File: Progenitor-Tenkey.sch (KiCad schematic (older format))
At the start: 208 parts, among them SW1 SW_Push, U1 ATmega32U4-AU, Y1 16MHz

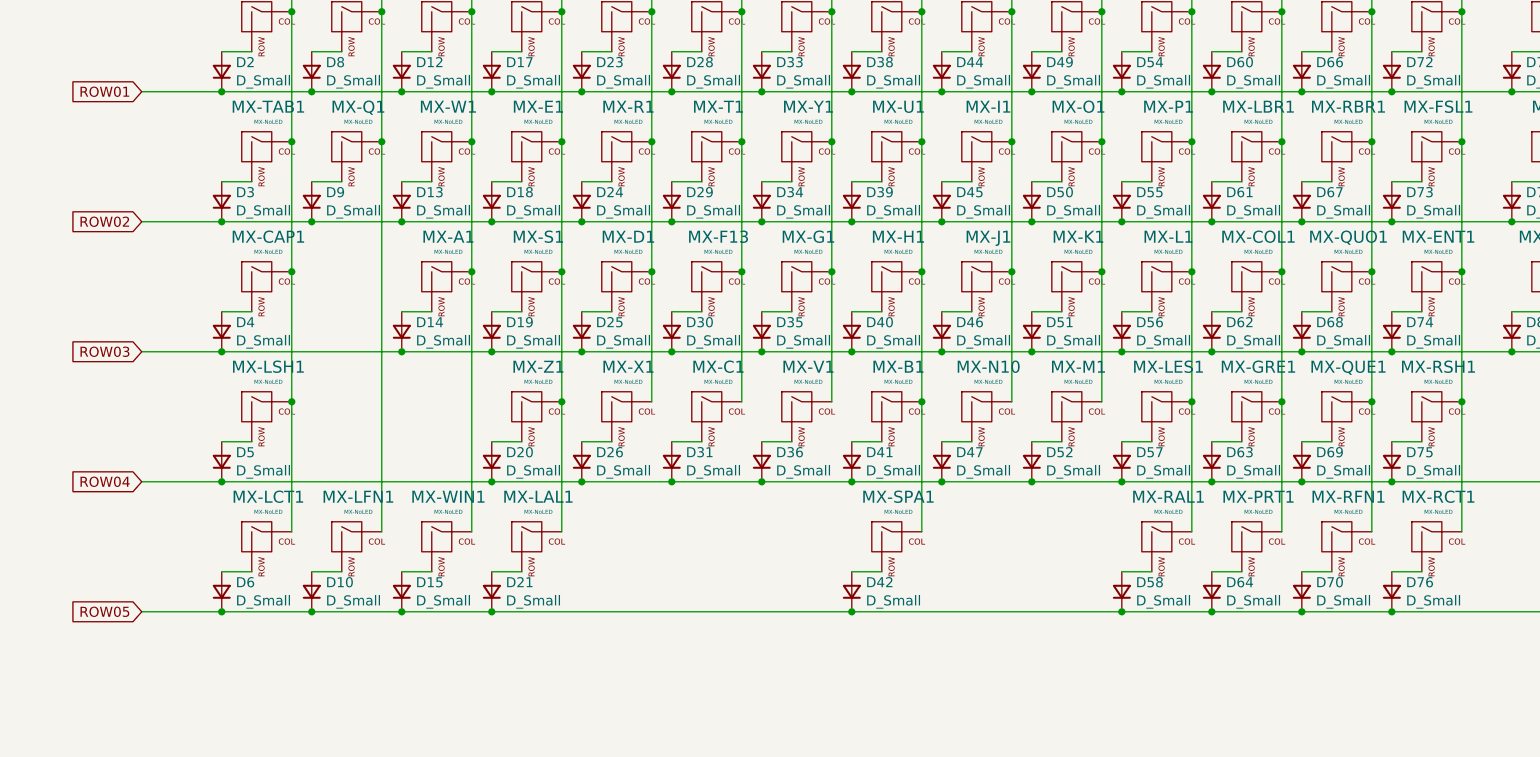
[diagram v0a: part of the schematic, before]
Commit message: Assigned Footprints
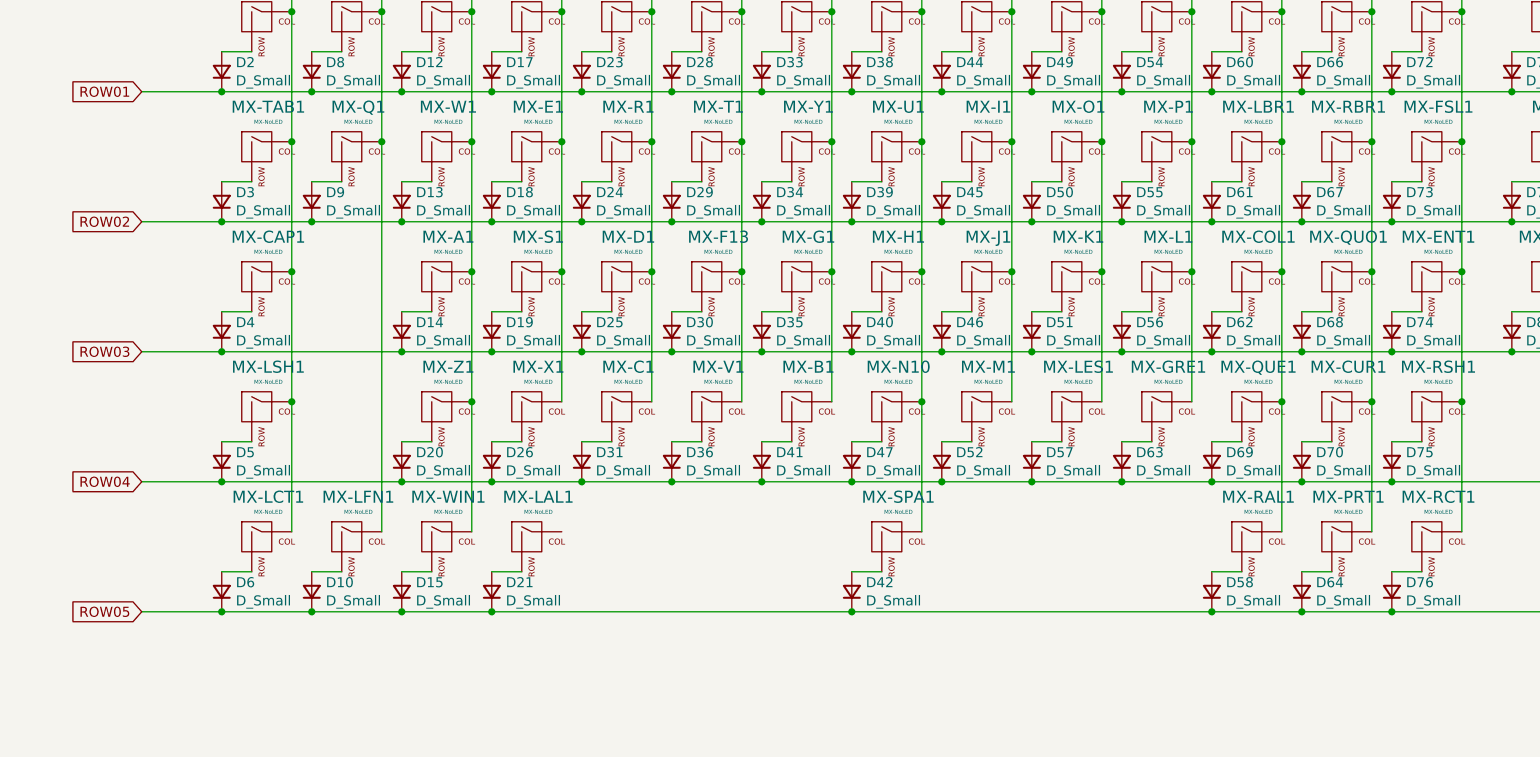
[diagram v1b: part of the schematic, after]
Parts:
- C1, C2, C3, C4, C5, C6, C7: footprint (none) -> Capacitor_SMD:C_0805_2012Metric
- D1, D10, D11, D12, D13, D14, D15, D16, D17, D18, D19, D2, D20, D21, D22, D23, D24, D25, D26, D27, D28, D29, D3, D30, D31, D32, D33, D34, D35, D36, D37, D38, D39, D4, D40, D41, D42, D43, D44, D45, D46, D47, D48, D49, D5, D50, D51, D52, D53, D54, D55, D56, D57, D58, D59, D6, D60, D61, D62, D63, D64, D65, D66, D67, D68, D69, D7, D70, D71, D72, D73, D74, D75, D76, D77, D78, D79, D8, D80, D81, D82, D83, D84, D85, D86, D87, D88, D89, D9, D90, D91, D92, D93, D94, D95, D96: footprint (none) -> Diode_SMD:D_SOD-123
- F1: footprint (none) -> Fuse:Fuse_1206_3216Metric
- MX-0, MX-1, MX-2, MX-3, MX-4, MX-5, MX-6, MX-7, MX-8, MX-9, MX-A1, MX-B1, MX-C1, MX-COL1, MX-D1, MX-DAR1, MX-DAS1, MX-E1, MX-ESC1, MX-F1, MX-F10, MX-F11, MX-F12, MX-F13, MX-F2, MX-F3, MX-F4, MX-F5, MX-F6, MX-F7, MX-F8, MX-F9, MX-FSL1, MX-G1, MX-GRE1, MX-H1, MX-I1, MX-J1, MX-K1, MX-L1, MX-LAL1, MX-LAR1, MX-LBR1, MX-LCT1, MX-LES1, MX-LFN1, MX-M1, MX-N0, MX-N1, MX-N10, MX-N2, MX-N3, MX-N4, MX-N5, MX-N6, MX-N7, MX-N8, MX-N9, MX-NAS1, MX-NDA1, MX-NDE1, MX-NPL1, MX-NSL1, MX-NUM1, MX-O1, MX-P1, MX-PLU1, MX-Q1, MX-QUE1, MX-QUO1, MX-R1, MX-RAR1, MX-RBR1, MX-S1, MX-T1, MX-TIL1, MX-U1, MX-UAR1, MX-V1, MX-W1, MX-WIN1, MX-X1, MX-Y1, MX-Z1: footprint (none) -> MX_Only:MXOnly-1U-NoLED
- MX-BAC1, MX-CAP1, MX-DEL1, MX-LSH1, MX-PRT1, MX-RCT1, MX-TAB1: footprint (none) -> MX_Only:MXOnly-1.5U-NoLED
- MX-CUR1: renamed from MX-RFN1; footprint (none) -> MX_Only:MXOnly-1U-NoLED
- MX-ENT1, MX-RSH1: footprint (none) -> MX_Only:MXOnly-2U-NoLED
- MX-RAL1: footprint (none) -> MX_Only:MXOnly-1.25U-NoLED
- MX-SPA1: footprint (none) -> MX_Only:MXOnly-6.25U-ReversedStabilizers-NoLED
- R1, R2, R3, R4: footprint (none) -> Resistor_SMD:R_0805_2012Metric
- SW1: footprint (none) -> random-keyboard-parts:SKQG-1155865
- USB1: footprint (none) -> random-keyboard-parts:Molex-0548190589
- Y1: footprint (none) -> Crystal:Crystal_SMD_3225-4Pin_3.2x2.5mm
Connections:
- net COL02: now also MX-Z1.1 (COL)
- net COL03: now also MX-X1.1 (COL); no longer MX-LAL1.1 (COL), MX-Z1.1 (COL)
- net COL04: now also MX-C1.1 (COL); no longer MX-X1.1 (COL)
- net COL05: now also MX-V1.1 (COL); no longer MX-C1.1 (COL)
- net COL06: now also MX-B1.1 (COL); no longer MX-V1.1 (COL)
- net COL07: now also MX-N10.1 (COL); no longer MX-B1.1 (COL)
- net COL08: now also MX-M1.1 (COL); no longer MX-N10.1 (COL)
- net COL09: now also MX-LES1.1 (COL); no longer MX-M1.1 (COL)
- net COL10: now also MX-GRE1.1 (COL); no longer MX-LES1.1 (COL), MX-RAL1.1 (COL)
- net COL11: now also MX-QUE1.1 (COL), MX-RAL1.1 (COL); no longer MX-GRE1.1 (COL), MX-PRT1.1 (COL)
- net COL12: now also MX-PRT1.1 (COL); no longer MX-QUE1.1 (COL)
- net ROW04: now also D70.1 (K)
- net ROW05: no longer D70.1 (K)
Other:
- moved on the sheet: D20, D26, D31, D36, D41, D47, D52, D57, D58, D63, D64, D69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

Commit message: Designed PCB Rev.1
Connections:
- net COL00: now also U1.18 (PD0); no longer U1.30 (PB6)
- net COL01: now also U1.19 (PD1); no longer U1.12 (PB7)
- net COL02: now also U1.21 (PD3); no longer U1.31 (PC6)
- net COL03: now also MX-LAL1.1 (COL), U1.22 (PD5); no longer U1.32 (PC7)
- net COL04: now also U1.25 (PD4); no longer U1.18 (PD0)
- net COL05: now also U1.26 (PD6); no longer U1.19 (PD1)
- net COL06: now also U1.27 (PD7); no longer U1.20 (PD2)
- net COL07: now also U1.28 (PB4); no longer U1.21 (PD3)
- net COL08: now also U1.1 (PE6); no longer U1.25 (PD4)
- net COL09: now also U1.36 (PF7); no longer U1.22 (PD5)
- net COL10: now also U1.37 (PF6); no longer U1.26 (PD6)
- net COL11: now also U1.38 (PF5); no longer U1.27 (PD7)
- net COL12: now also U1.39 (PF4); no longer U1.41 (PF0)
- net COL14: now also U1.11 (PB3); no longer U1.39 (PF4)
- net COL15: now also U1.29 (PB5); no longer U1.38 (PF5)
- net COL16: now also U1.30 (PB6); no longer U1.37 (PF6)
- net COL17: now also U1.31 (PC6); no longer U1.36 (PF7)
- net ROW03: now also U1.12 (PB7); no longer U1.11 (PB3)
- net ROW04: now also U1.41 (PF0); no longer U1.28 (PB4)
- net ROW05: now also U1.32 (PC7); no longer U1.29 (PB5)
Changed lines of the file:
@@
 Text GLabel 3250 1600 2    50   Input ~ 0
 ROW02
-Text GLabel 3250 1700 2    50   Input ~ 0
-ROW03
+Text GLabel 3250 3800 2    50   Input ~ 0
+ROW04
+Text GLabel 3250 2600 2    50   Input ~ 0
+COL00
+Text GLabel 3250 2700 2    50   Input ~ 0
+COL01
+Text GLabel 3250 2900 2    50   Input ~ 0
+COL02
+Text GLabel 3250 3100 2    50   Input ~ 0
+COL03
+Text GLabel 3250 3000 2    50   Input ~ 0
+COL04
+Text GLabel 3250 3200 2    50   Input ~ 0
+COL05
+Text GLabel 3250 3300 2    50   Input ~ 0
+COL06
 Text GLabel 3250 1800 2    50   Input ~ 0
-ROW04
-Text GLabel 3250 1900 2    50   Input ~ 0
-ROW05
-Text GLabel 3250 2000 2    50   Input ~ 0
-COL00
-Text GLabel 3250 2100 2    50   Input ~ 0
-COL01
-Text GLabel 3250 2300 2    50   Input ~ 0
-COL02
-Text GLabel 3250 2400 2    50   Input ~ 0
-COL03
-Text GLabel 3250 2600 2    50   Input ~ 0
-COL04
-Text GLabel 3250 2700 2    50   Input ~ 0
-COL05
-Text GLabel 3250 2800 2    50   Input ~ 0
-COL06
-Text GLabel 3250 2900 2    50   Input ~ 0
 COL07
-Text GLabel 3250 3000 2    50   Input ~ 0
+Text GLabel 3250 3600 2    50   Input ~ 0
 COL08
-Text GLabel 3250 3100 2    50   Input ~ 0
+Text GLabel 3250 4300 2    50   Input ~ 0
 COL09
-Text GLabel 3250 3200 2    50   Input ~ 0
+Text GLabel 3250 4200 2    50   Input ~ 0
 COL10
-Text GLabel 3250 3300 2    50   Input ~ 0
+Text GLabel 3250 4100 2    50   Input ~ 0
 COL11
-Text GLabel 3250 3800 2    50   Input ~ 0
+Text GLabel 3250 4000 2    50   Input ~ 0
 COL12
 Text GLabel 3250 3900 2    50   Input ~ 0
 COL13
-Text GLabel 3250 4000 2    50   Input ~ 0
+Text GLabel 3250 1700 2    50   Input ~ 0
 COL14
-Text GLabel 3250 4100 2    50   Input ~ 0
+Text GLabel 3250 1900 2    50   Input ~ 0
 COL15
-Text GLabel 3250 4200 2    50   Input ~ 0
-COL16
-Text GLabel 3250 4300 2    50   Input ~ 0
+Text GLabel 3250 2300 2    50   Input ~ 0
 COL17
 Wire Wire Line
@@
 Wire Wire Line
 	6300 4550 5400 4550
+Wire Wire Line
+	7100 4800 7100 4150
+Connection ~ 7100 4150
+Text GLabel 3250 2100 2    50   Input ~ 0
+ROW03
+Text GLabel 3250 2400 2    50   Input ~ 0
+ROW05
+Text GLabel 3250 2000 2    50   Input ~ 0
+COL16
 $EndSCHEMATC

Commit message: Small Tweaks
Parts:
- USB1: value Molex-0548190519 -> Molex-0548190589; symbol random-keyboard-parts:Molex-0548190519 -> random-keyboard-parts:Molex-0548190589
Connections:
- net GND: now also USB1.6 (SHIELD)
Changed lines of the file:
@@
 D-
 $Comp
-L random-keyboard-parts:Molex-0548190519 USB1
+L random-keyboard-parts:Molex-0548190589 USB1
 U 1 1 60750D63
 P 950 5550
 F 0 "USB1" V 1487 5517 60  0000 C CNN
-F 1 "Molex-0548190519" V 1381 5517 60  0000 C CNN
+F 1 "Molex-0548190589" V 1381 5517 60  0000 C CNN
 F 2 "random-keyboard-parts:Molex-0548190589" H 950 5550 60  0001 C CNN
 F 3 "" H 950 5550 60  0001 C CNN
@@
 Text GLabel 3250 2000 2    50   Input ~ 0
 COL16
+Wire Wire Line
+	1250 5250 1250 5150
+Wire Wire Line
+	1250 5150 1350 5150
+$Comp
+L power:GND #PWR0114
+U 1 1 60777F8A
+P 1350 5150
+F 0 "#PWR0114" H 1350 4900 50  0001 C CNN
+F 1 "GND" H 1355 4977 50  0000 C CNN
+F 2 "" H 1350 5150 50  0001 C CNN
+F 3 "" H 1350 5150 50  0001 C CNN
+	1    1350 5150
+	1    0    0    -1
+$EndComp
 $EndSCHEMATC

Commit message: More tweaks, regenerated Gerber
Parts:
- R1, R2: value R_Small -> 22
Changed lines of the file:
@@
 P 1650 2400
 F 0 "R2" V 1454 2400 50  0000 C CNN
-F 1 "R_Small" V 1545 2400 50  0000 C CNN
+F 1 "22" V 1545 2400 50  0000 C CNN
 F 2 "Resistor_SMD:R_0805_2012Metric" H 1650 2400 50  0001 C CNN
 F 3 "~" H 1650 2400 50  0001 C CNN
@@
 P 1350 2500
 F 0 "R1" V 1154 2500 50  0000 C CNN
-F 1 "R_Small" V 1245 2500 50  0000 C CNN
+F 1 "22" V 1245 2500 50  0000 C CNN
 F 2 "Resistor_SMD:R_0805_2012Metric" H 1350 2500 50  0001 C CNN
 F 3 "~" H 1350 2500 50  0001 C CNN
